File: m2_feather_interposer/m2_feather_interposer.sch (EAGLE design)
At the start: 61 parts, among them J1 RICKK2_SPARK_M.2EKEY, U2 BQ24195, U3 MAX1704X, U6 XC9258A33EER-G, U7 XC8107SOT25

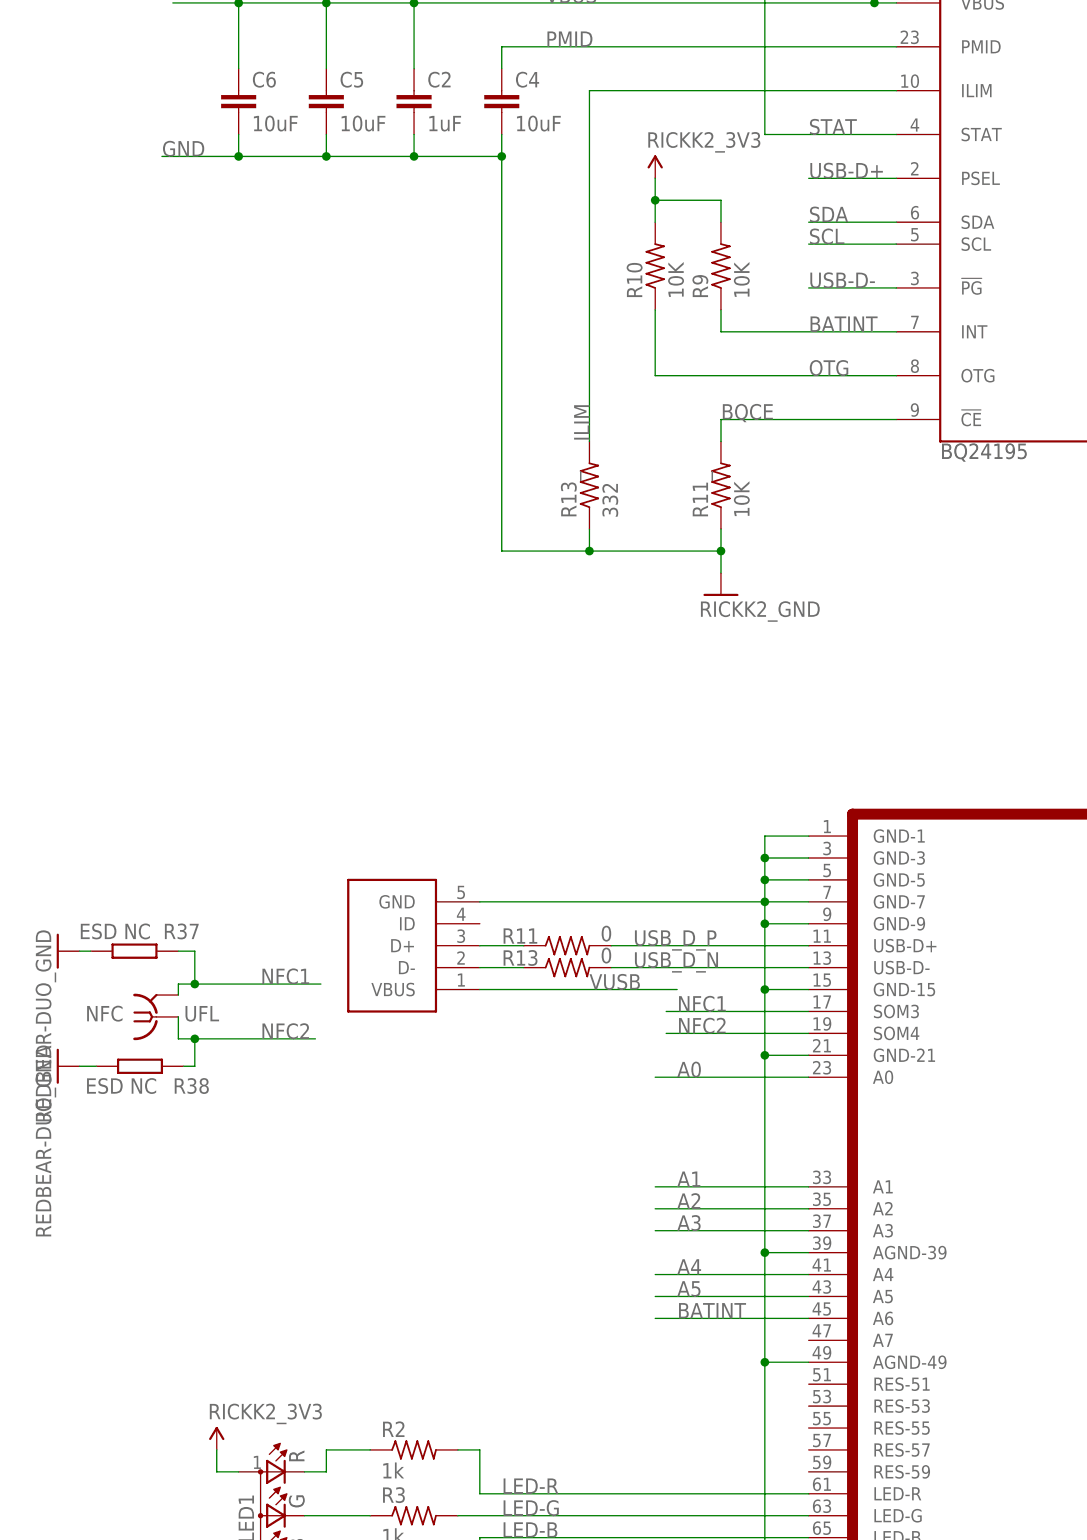
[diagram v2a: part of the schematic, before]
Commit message: GPIO:draft layout done, LED: draft layout done, Buttons:draft layout done, SIM: draft layout done, NFC: draft layout done. Open items: fuel gauge, pmic, 3.3V reg
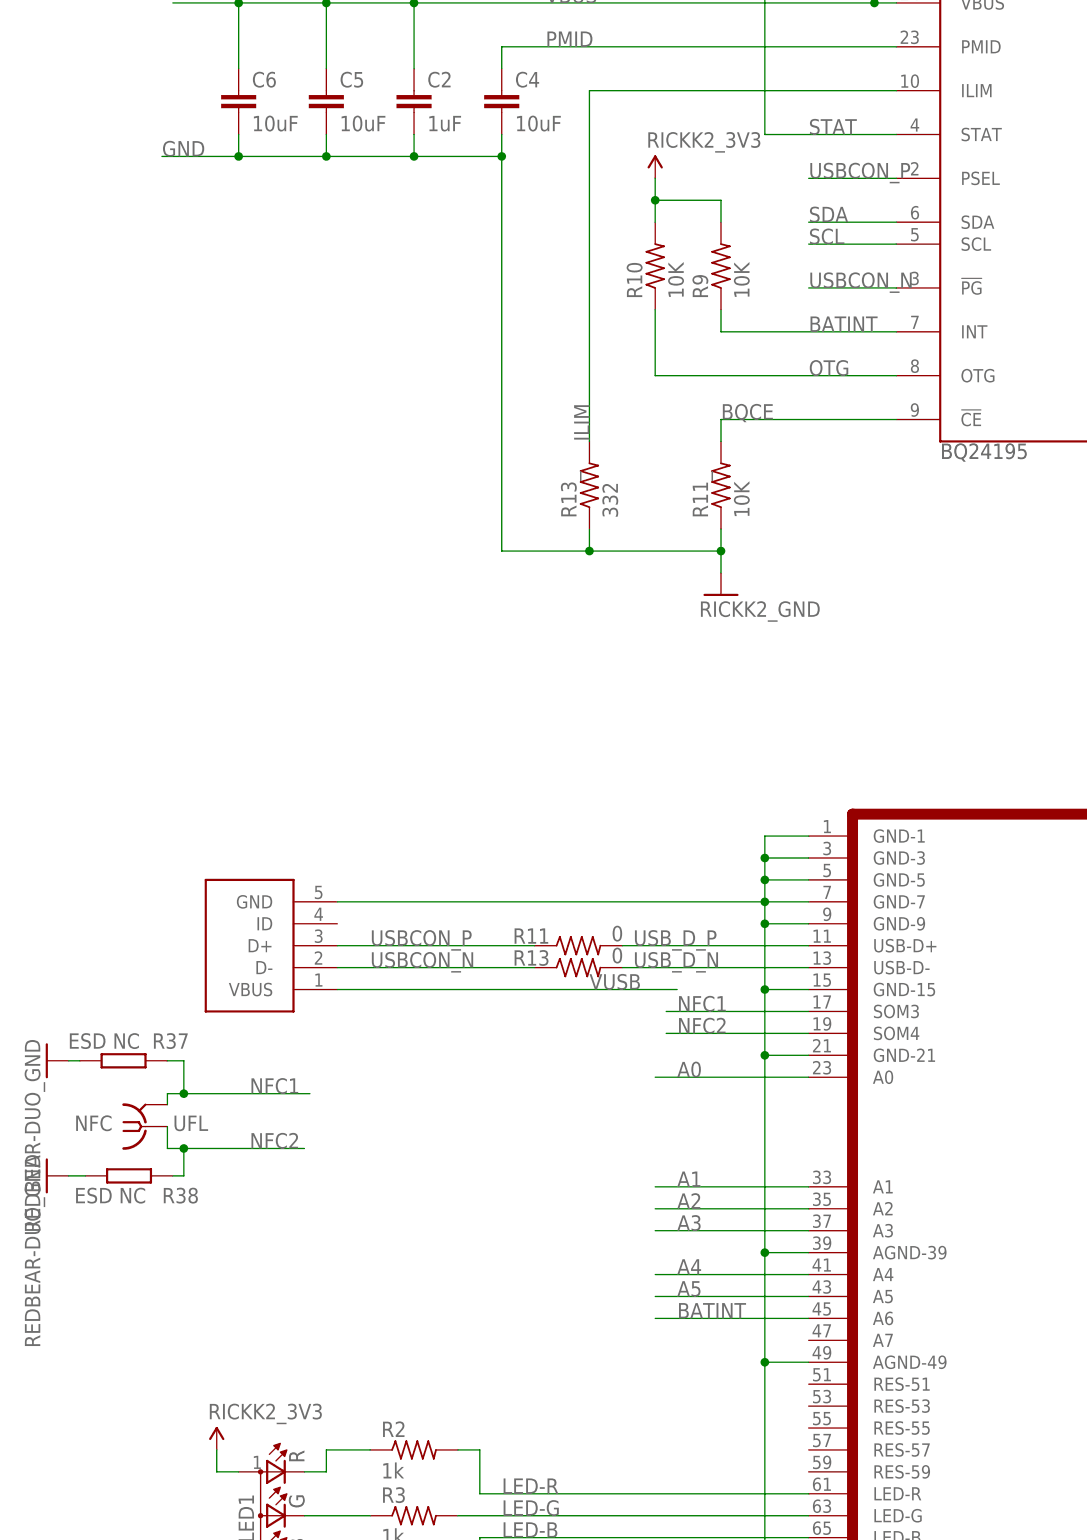
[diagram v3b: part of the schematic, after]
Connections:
- removed net N$4: R11.1, U$3.D+
- removed net N$8: R13.1, U$3.D-
- removed net USB-D+: U2.PSEL
- removed net USB-D-: U2.!PG
- new net USBCON_N: R13.1, U$3.D-, U2.!PG
- new net USBCON_P: R11.1, U$3.D+, U2.PSEL
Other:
- moved on the sheet: NFC, R11, R13, R37, R38
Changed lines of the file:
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@@
 <attribute name="VALUE" x="116.84" y="-22.86" size="1.778" layer="96"/>
 </instance>
-<instance part="U$3" gate="G$1" x="-2.54" y="78.74" smashed="yes" rot="R180"/>
+<instance part="U$3" gate="G$1" x="-19.05" y="78.74" smashed="yes" rot="R180"/>
 <instance part="SUPPLY1" gate="G$1" x="124.46" y="66.04" smashed="yes">
 <attribute name="VALUE" x="123.444" y="69.596" size="1.778" layer="96"/>
@@
 </instance>
 <instance part="U$1" gate="G$1" x="81.28" y="-22.86" smashed="yes"/>
-<instance part="NFC" gate="G$1" x="-32.385" y="67.945" smashed="yes" rot="MR180">
-<attribute name="VALUE" x="-29.21" y="69.215" size="1.778" layer="96" rot="MR180"/>
-<attribute name="NAME" x="-36.195" y="67.437" size="1.778" layer="95" rot="MR0"/>
-</instance>
-<instance part="R37" gate="G$1" x="-34.925" y="75.565" smashed="yes" rot="R180">
-<attribute name="NAME" x="-27.305" y="78.74" size="1.778" layer="95" rot="R180"/>
-<attribute name="VALUE" x="-33.02" y="78.74" size="1.778" layer="96" rot="R180"/>
-</instance>
-<instance part="R38" gate="G$1" x="-34.29" y="62.23" smashed="yes">
-<attribute name="NAME" x="-30.48" y="59.055" size="1.778" layer="95"/>
-<attribute name="VALUE" x="-40.64" y="59.055" size="1.778" layer="96"/>
-</instance>
-<instance part="GND60" gate="1" x="-43.815" y="75.565" smashed="yes" rot="R270">
-<attribute name="VALUE" x="-46.355" y="78.105" size="1.778" layer="96" rot="R270"/>
-</instance>
-<instance part="GND62" gate="1" x="-43.815" y="62.23" smashed="yes" rot="R270">
-<attribute name="VALUE" x="-46.355" y="64.77" size="1.778" layer="96" rot="R270"/>
+<instance part="NFC" gate="G$1" x="-33.655" y="55.245" smashed="yes" rot="MR180">
+<attribute name="VALUE" x="-30.48" y="56.515" size="1.778" layer="96" rot="MR180"/>
+<attribute name="NAME" x="-37.465" y="54.737" size="1.778" layer="95" rot="MR0"/>
+</instance>
+<instance part="R37" gate="G$1" x="-36.195" y="62.865" smashed="yes" rot="R180">
+<attribute name="NAME" x="-28.575" y="66.04" size="1.778" layer="95" rot="R180"/>
+<attribute name="VALUE" x="-34.29" y="66.04" size="1.778" layer="96" rot="R180"/>
+</instance>
+<instance part="R38" gate="G$1" x="-35.56" y="49.53" smashed="yes">
+<attribute name="NAME" x="-31.75" y="46.355" size="1.778" layer="95"/>
+<attribute name="VALUE" x="-41.91" y="46.355" size="1.778" layer="96"/>
+</instance>
+<instance part="GND60" gate="1" x="-45.085" y="62.865" smashed="yes" rot="R270">
+<attribute name="VALUE" x="-47.625" y="65.405" size="1.778" layer="96" rot="R270"/>
+</instance>
+<instance part="GND62" gate="1" x="-45.085" y="49.53" smashed="yes" rot="R270">
+<attribute name="VALUE" x="-47.625" y="52.07" size="1.778" layer="96" rot="R270"/>
 </instance>
 <instance part="MS1" gate="G$1" x="215.9" y="38.1" smashed="yes" rot="R270"/>
@@
 <attribute name="VALUE" x="68.58" y="-78.232" size="1.778" layer="96"/>
 </instance>
-<instance part="R11" gate="G$1" x="15.24" y="76.2" smashed="yes">
-<attribute name="NAME" x="7.62" y="76.4286" size="1.778" layer="95"/>
-<attribute name="VALUE" x="19.05" y="76.708" size="1.778" layer="96"/>
-</instance>
-<instance part="R13" gate="G$1" x="15.24" y="73.66" smashed="yes">
-<attribute name="NAME" x="7.62" y="73.8886" size="1.778" layer="95"/>
-<attribute name="VALUE" x="19.05" y="74.168" size="1.778" layer="96"/>
+<instance part="R11" gate="G$1" x="16.51" y="76.2" smashed="yes">
+<attribute name="NAME" x="8.89" y="76.4286" size="1.778" layer="95"/>
+<attribute name="VALUE" x="20.32" y="76.708" size="1.778" layer="96"/>
+</instance>
+<instance part="R13" gate="G$1" x="16.51" y="73.66" smashed="yes">
+<attribute name="NAME" x="8.89" y="73.8886" size="1.778" layer="95"/>
+<attribute name="VALUE" x="20.32" y="74.168" size="1.778" layer="96"/>
 </instance>
 </instances>
@@
 <junction x="38.1" y="71.12"/>
 <pinref part="U$3" gate="G$1" pin="GND"/>
-<wire x1="5.08" y1="81.28" x2="38.1" y2="81.28" width="0.1524" layer="91"/>
+<wire x1="-11.43" y1="81.28" x2="38.1" y2="81.28" width="0.1524" layer="91"/>
 <pinref part="J1" gate="G$1" pin="GND-1"/>
 <pinref part="J1" gate="G$1" pin="GND-3"/>
@@
 <pinref part="R37" gate="G$1" pin="2"/>
 <pinref part="GND60" gate="1" pin="GND"/>
-<wire x1="-40.005" y1="75.565" x2="-41.275" y2="75.565" width="0.1524" layer="91"/>
+<wire x1="-41.275" y1="62.865" x2="-42.545" y2="62.865" width="0.1524" layer="91"/>
 </segment>
 <segment>
 <pinref part="R38" gate="G$1" pin="1"/>
 <pinref part="GND62" gate="1" pin="GND"/>
-<wire x1="-39.37" y1="62.23" x2="-41.275" y2="62.23" width="0.1524" layer="91"/>
+<wire x1="-40.64" y1="49.53" x2="-42.545" y2="49.53" width="0.1524" layer="91"/>
 </segment>
 <segment>
@@
 <pinref part="J1" gate="G$1" pin="LED-B"/>
 <pinref part="R4" gate="G$1" pin="2"/>
-</segment>
-</net>
-<net name="USB-D+" class="1">
-<segment>
-<pinref part="U2" gate="G$1" pin="PSEL"/>
-<wire x1="53.34" y1="165.1" x2="43.18" y2="165.1" width="0.1524" layer="91"/>
-<label x="43.18" y="165.1" size="1.778" layer="95"/>
-</segment>
-</net>
-<net name="USB-D-" class="1">
-<segment>
-<pinref part="U2" gate="G$1" pin="!PG"/>
-<wire x1="53.34" y1="152.4" x2="43.18" y2="152.4" width="0.1524" layer="91"/>
-<label x="43.18" y="152.4" size="1.778" layer="95"/>
 </segment>
 </net>
@@
 <segment>
 <pinref part="U$3" gate="G$1" pin="VBUS"/>
-<wire x1="5.08" y1="71.12" x2="27.94" y2="71.12" width="0.1524" layer="91"/>
+<wire x1="-11.43" y1="71.12" x2="27.94" y2="71.12" width="0.1524" layer="91"/>
 <label x="17.78" y="71.12" size="1.778" layer="95"/>
 </segment>
@@
 <segment>
 <pinref part="NFC" gate="G$1" pin="GND@1"/>
-<wire x1="-29.845" y1="70.485" x2="-29.845" y2="71.755" width="0.1524" layer="91"/>
-<wire x1="-29.845" y1="71.755" x2="-27.94" y2="71.755" width="0.1524" layer="91"/>
+<wire x1="-31.115" y1="57.785" x2="-31.115" y2="59.055" width="0.1524" layer="91"/>
+<wire x1="-31.115" y1="59.055" x2="-29.21" y2="59.055" width="0.1524" layer="91"/>
 <pinref part="R37" gate="G$1" pin="1"/>
-<wire x1="-29.845" y1="75.565" x2="-27.94" y2="75.565" width="0.1524" layer="91"/>
-<wire x1="-27.94" y1="75.565" x2="-27.94" y2="71.755" width="0.1524" layer="91"/>
-<junction x="-27.94" y="71.755"/>
-<wire x1="-27.94" y1="71.755" x2="-13.335" y2="71.755" width="0.1524" layer="91"/>
-<label x="-20.32" y="71.755" size="1.778" layer="95"/>
+<wire x1="-31.115" y1="62.865" x2="-29.21" y2="62.865" width="0.1524" layer="91"/>
+<wire x1="-29.21" y1="62.865" x2="-29.21" y2="59.055" width="0.1524" layer="91"/>
+<junction x="-29.21" y="59.055"/>
+<wire x1="-29.21" y1="59.055" x2="-14.605" y2="59.055" width="0.1524" layer="91"/>
+<label x="-21.59" y="59.055" size="1.778" layer="95"/>
 </segment>
 <segment>
@@
 <segment>
 <pinref part="NFC" gate="G$1" pin="1"/>
-<wire x1="-27.94" y1="65.405" x2="-29.845" y2="65.405" width="0.1524" layer="91"/>
-<wire x1="-29.845" y1="67.945" x2="-29.845" y2="65.405" width="0.1524" layer="91"/>
+<wire x1="-29.21" y1="52.705" x2="-31.115" y2="52.705" width="0.1524" layer="91"/>
+<wire x1="-31.115" y1="55.245" x2="-31.115" y2="52.705" width="0.1524" layer="91"/>
 <pinref part="R38" gate="G$1" pin="2"/>
-<wire x1="-29.21" y1="62.23" x2="-27.94" y2="62.23" width="0.1524" layer="91"/>
-<wire x1="-27.94" y1="62.23" x2="-27.94" y2="65.405" width="0.1524" layer="91"/>
-<junction x="-27.94" y="65.405"/>
-<wire x1="-27.94" y1="65.405" x2="-13.97" y2="65.405" width="0.1524" layer="91"/>
-<label x="-20.32" y="65.405" size="1.778" layer="95"/>
+<wire x1="-30.48" y1="49.53" x2="-29.21" y2="49.53" width="0.1524" layer="91"/>
+<wire x1="-29.21" y1="49.53" x2="-29.21" y2="52.705" width="0.1524" layer="91"/>
+<junction x="-29.21" y="52.705"/>
+<wire x1="-29.21" y1="52.705" x2="-15.24" y2="52.705" width="0.1524" layer="91"/>
+<label x="-21.59" y="52.705" size="1.778" layer="95"/>
 </segment>
 <segment>
@@
 </segment>
 </net>
-<net name="N$4" class="1">
+<net name="USBCON_P" class="1">
 <segment>
 <pinref part="U$3" gate="G$1" pin="D+"/>
 <pinref part="R11" gate="G$1" pin="1"/>
-<wire x1="5.08" y1="76.2" x2="10.16" y2="76.2" width="0.1524" layer="91"/>
-</segment>
-</net>
-<net name="N$8" class="1">
+<wire x1="-11.43" y1="76.2" x2="11.43" y2="76.2" width="0.1524" layer="91"/>
+<label x="-7.62" y="76.2" size="1.778" layer="95"/>
+</segment>
+<segment>
+<pinref part="U2" gate="G$1" pin="PSEL"/>
+<wire x1="53.34" y1="165.1" x2="43.18" y2="165.1" width="0.1524" layer="91"/>
+<label x="43.18" y="165.1" size="1.778" layer="95"/>
+</segment>
+</net>
+<net name="USBCON_N" class="1">
 <segment>
 <pinref part="U$3" gate="G$1" pin="D-"/>
 <pinref part="R13" gate="G$1" pin="1"/>
-<wire x1="5.08" y1="73.66" x2="10.16" y2="73.66" width="0.1524" layer="91"/>
+<wire x1="-11.43" y1="73.66" x2="11.43" y2="73.66" width="0.1524" layer="91"/>
+<label x="-7.62" y="73.66" size="1.778" layer="95"/>
+</segment>
+<segment>
+<pinref part="U2" gate="G$1" pin="!PG"/>
+<wire x1="53.34" y1="152.4" x2="43.18" y2="152.4" width="0.1524" layer="91"/>
+<label x="43.18" y="152.4" size="1.778" layer="95"/>
 </segment>
 </net>
@@
 <pinref part="R11" gate="G$1" pin="2"/>
 <pinref part="J1" gate="G$1" pin="USB-D+"/>
-<wire x1="20.32" y1="76.2" x2="43.18" y2="76.2" width="0.1524" layer="91"/>
+<wire x1="21.59" y1="76.2" x2="43.18" y2="76.2" width="0.1524" layer="91"/>
 <label x="22.86" y="76.2" size="1.778" layer="95"/>
 </segment>
@@
 <pinref part="R13" gate="G$1" pin="2"/>
 <pinref part="J1" gate="G$1" pin="USB-D-"/>
-<wire x1="20.32" y1="73.66" x2="43.18" y2="73.66" width="0.1524" layer="91"/>
+<wire x1="21.59" y1="73.66" x2="43.18" y2="73.66" width="0.1524" layer="91"/>
 <label x="22.86" y="73.66" size="1.778" layer="95"/>
 </segment>

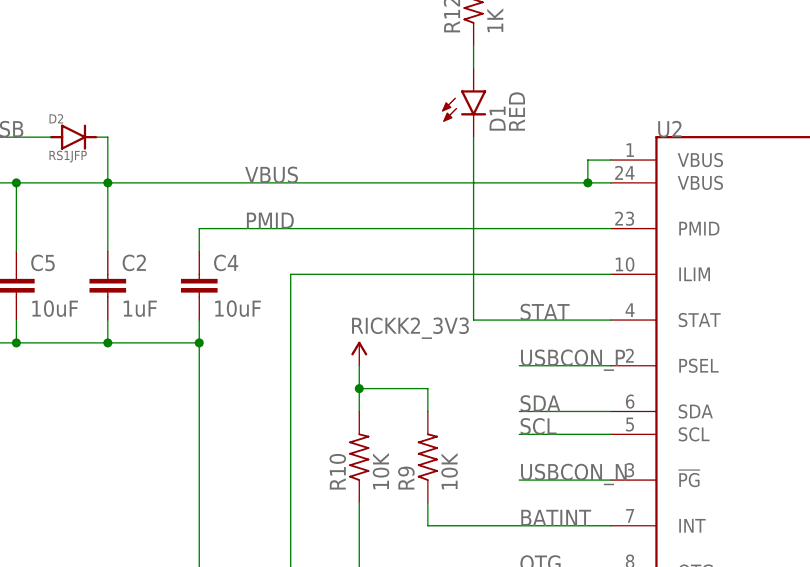
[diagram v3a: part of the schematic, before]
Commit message: working through pmic, 3.3V and pwr switch layout:
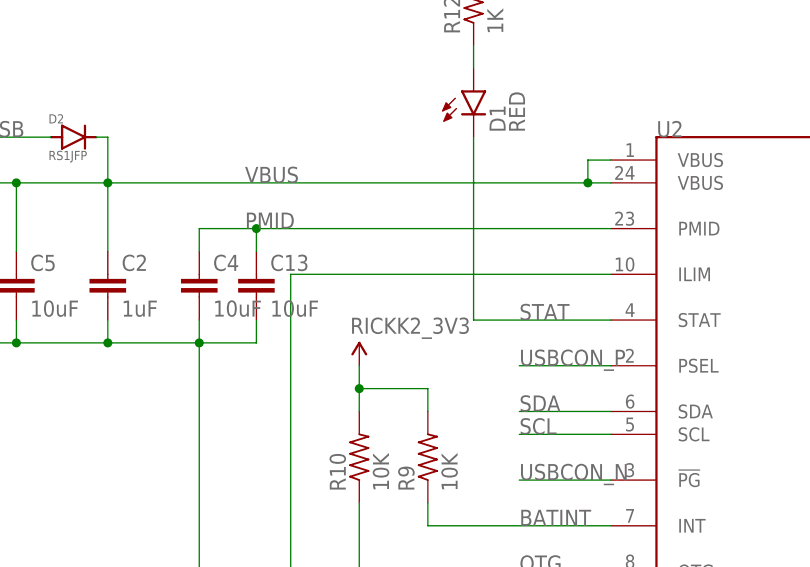
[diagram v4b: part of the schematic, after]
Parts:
- added C13: 10uF, m2_feather_interposer:RICKK2_CAP-10UF-0603
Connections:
- net GND: now also C13.2
- net PMID: now also C13.1
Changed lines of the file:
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@@
 <part name="R11" library="adafruit" library_urn="urn:adsk.eagle:library:420" deviceset="R-US_" device="R0402" package3d_urn="urn:adsk.eagle:package:6240564/1" value="0"/>
 <part name="R13" library="adafruit" library_urn="urn:adsk.eagle:library:420" deviceset="R-US_" device="R0402" package3d_urn="urn:adsk.eagle:package:6240564/1" value="0"/>
+<part name="C13" library="m2_feather_interposer" deviceset="RICKK2_CAP-10UF-0603" device="" value="10uF"/>
 </parts>
 <sheets>
@@
 <attribute name="NAME" x="8.89" y="73.8886" size="1.778" layer="95"/>
 <attribute name="VALUE" x="20.32" y="74.168" size="1.778" layer="96"/>
+</instance>
+<instance part="C13" gate="G$1" x="13.97" y="172.72" smashed="yes">
+<attribute name="NAME" x="15.494" y="175.641" size="1.778" layer="95"/>
+<attribute name="VALUE" x="15.494" y="170.561" size="1.778" layer="96"/>
 </instance>
 </instances>
@@
 <pinref part="R13_" gate="G$1" pin="1"/>
 <pinref part="R11_" gate="G$1" pin="1"/>
+<pinref part="C13" gate="G$1" pin="2"/>
+<wire x1="13.97" y1="170.18" x2="13.97" y2="167.64" width="0.1524" layer="91"/>
+<wire x1="13.97" y1="167.64" x2="7.62" y2="167.64" width="0.1524" layer="91"/>
 </segment>
 <segment>
@@
 <segment>
 <pinref part="U2" gate="G$1" pin="PMID"/>
-<wire x1="53.34" y1="180.34" x2="7.62" y2="180.34" width="0.1524" layer="91"/>
+<wire x1="53.34" y1="180.34" x2="13.97" y2="180.34" width="0.1524" layer="91"/>
 <pinref part="C4" gate="G$1" pin="1"/>
+<wire x1="13.97" y1="180.34" x2="7.62" y2="180.34" width="0.1524" layer="91"/>
 <wire x1="7.62" y1="180.34" x2="7.62" y2="177.8" width="0.1524" layer="91"/>
 <label x="12.7" y="180.34" size="1.778" layer="95"/>
-</segment>
-</net>
+<pinref part="C13" gate="G$1" pin="1"/>
+<wire x1="13.97" y1="177.8" x2="13.97" y2="180.34" width="0.1524" layer="91"/>
+<junction x="13.97" y="180.34"/>
+</segment>
+</net>
